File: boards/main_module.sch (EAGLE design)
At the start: 15 parts, among them IC1 K155ID1

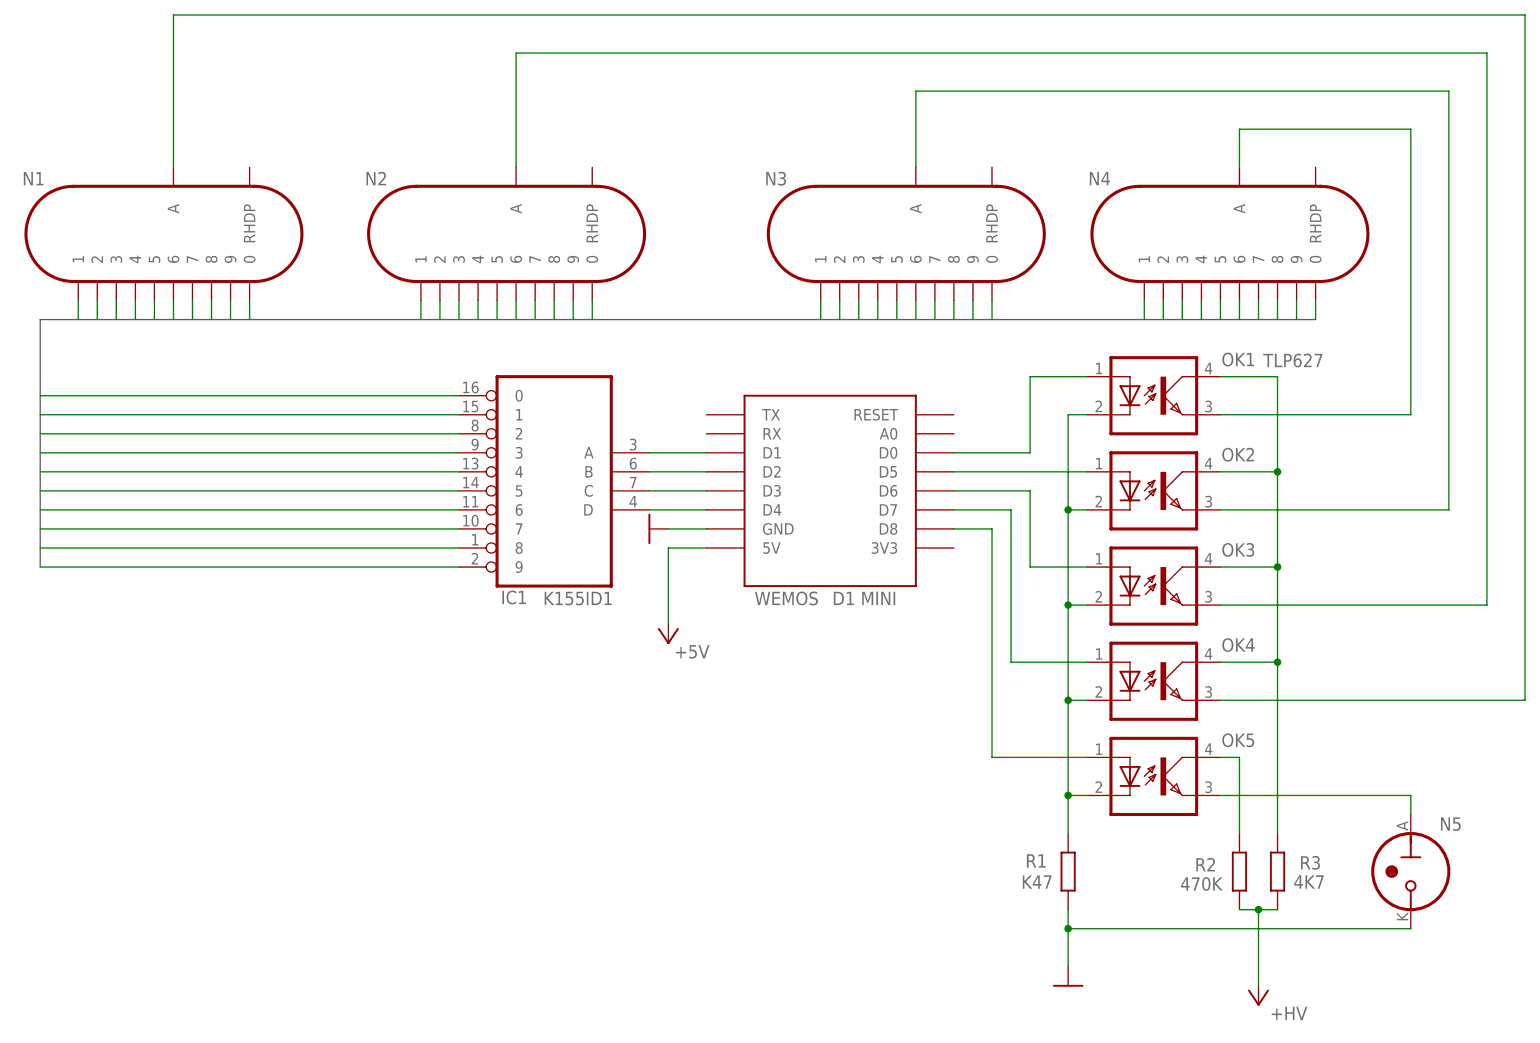
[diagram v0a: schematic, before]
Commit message: Complete schematic of the main module
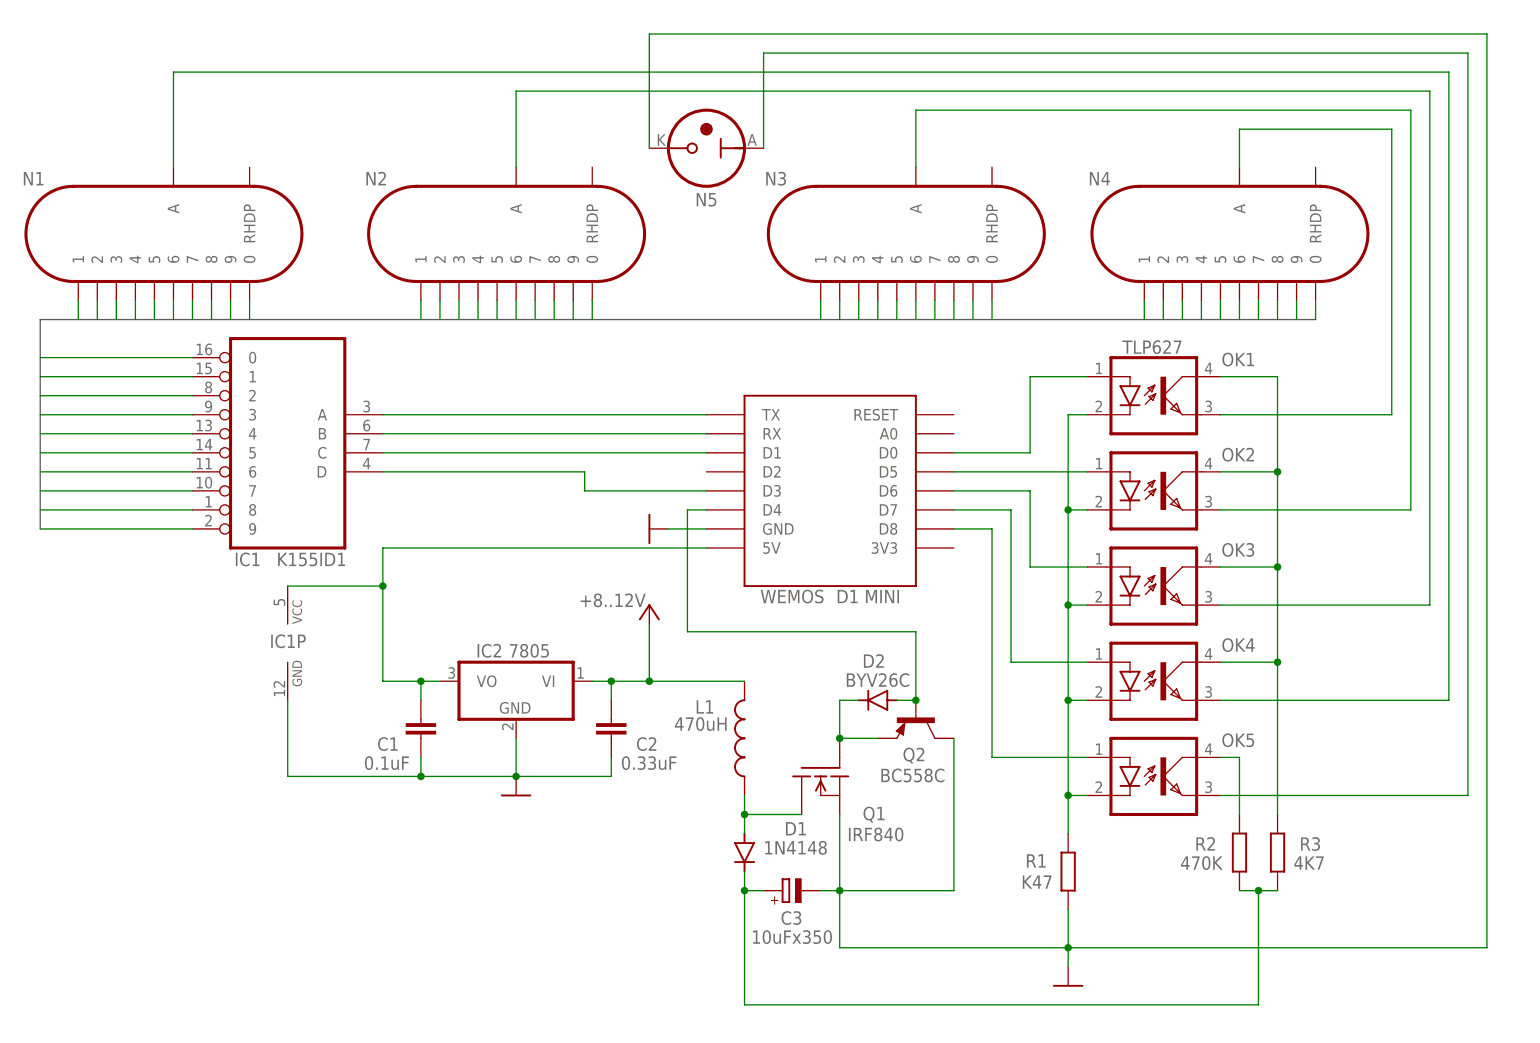
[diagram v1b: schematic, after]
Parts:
- added C1: 0.1uF, rcl:C-EU075-052X106
- added C2: 0.33uF, rcl:C-EU075-052X106
- added C3: 10uFx350, rcl:CPOL-EUE5-10.5
- added D1: 1N4148, diode:1N4148DO35-10
- added D2: BYV26C, diode:BYV27
- added IC2: 7805, linear:7805T
- added L1: 470uH, rcl:L-US6000-XXX-RC
- added Q1: IRF840, transistor-fet:IRF840
- added Q2: BC558C, transistor-pnp:BC558C
- R1, R2, R3: device rcl:R-EU_0207/10 -> rcl:R-EU_0207/12
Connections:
- removed net +5V: WEMOS.5V
- new net N$18: C1.1, IC1P.VCC, IC2.VO, WEMOS.5V
- new net N$19: D2.C, Q1.G, Q2.E
- new net N$20: D1.A, L1.1, Q1.D
- new net N$21: C3.+, D1.C, R2.1, R3.1
- new net N$23: D2.A, Q2.B, WEMOS.D4
- net GND: now also C1.2, C2.2, C3.-, IC1P.GND, IC2.GND, Q1.S, Q2.C
- net N$1: now also WEMOS.TX; no longer WEMOS.D1
- net N$2: now also WEMOS.RX; no longer WEMOS.D2
- net N$3: now also WEMOS.D1; no longer WEMOS.D3
- net N$4: now also WEMOS.D3; no longer WEMOS.D4
- net N8: no longer N1.9
- net N9: now also N1.9
- net VCC: now also C2.1, IC2.VI, L1.2; no longer R2.1, R3.1
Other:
- moved on the sheet: IC1, N5, R2, R3
